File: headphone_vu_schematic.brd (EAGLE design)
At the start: 100 x 80 mm, 20 parts, among them IC1 LM3914V

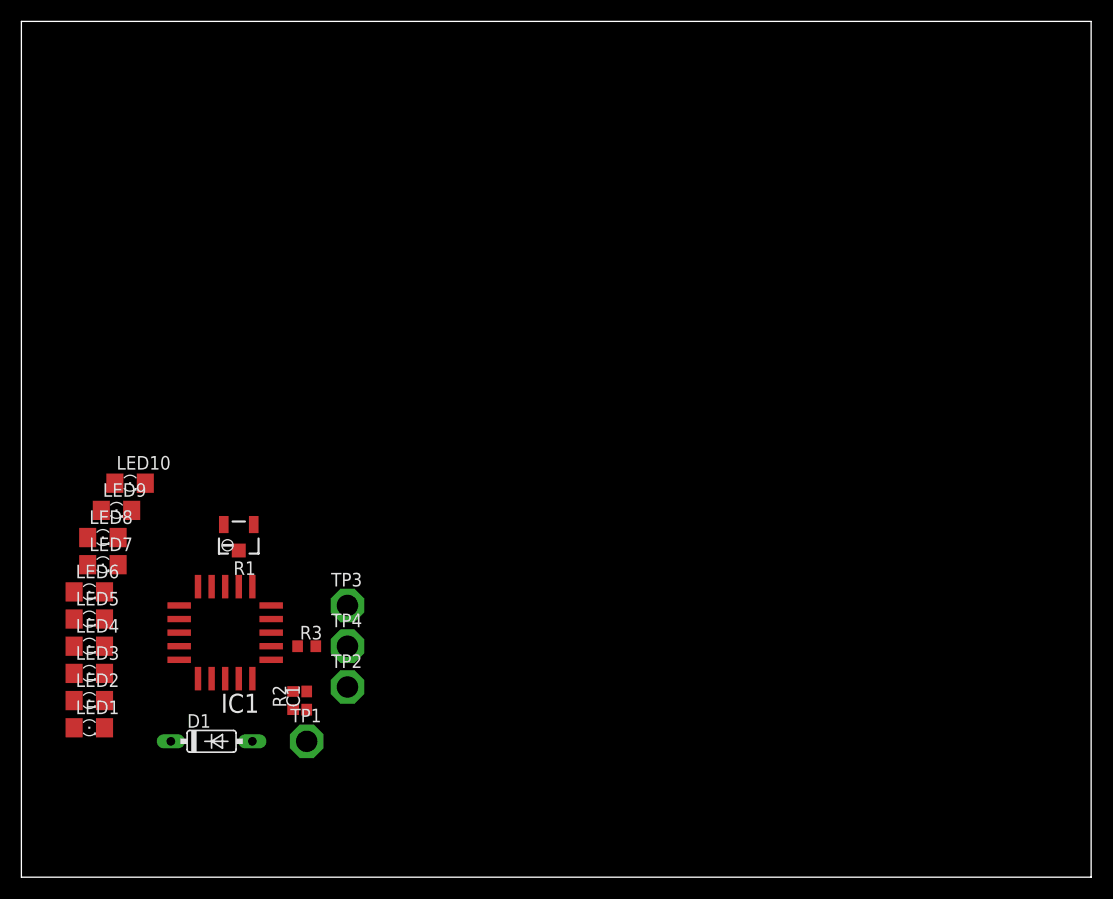
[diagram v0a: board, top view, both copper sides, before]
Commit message: Finished Board
Routed the board.  Everything seems to be in good order.  Single layer,
10 mil min width, 16 mil spacing.  Its hassling me saying there's a
ground not connected, but its all there.
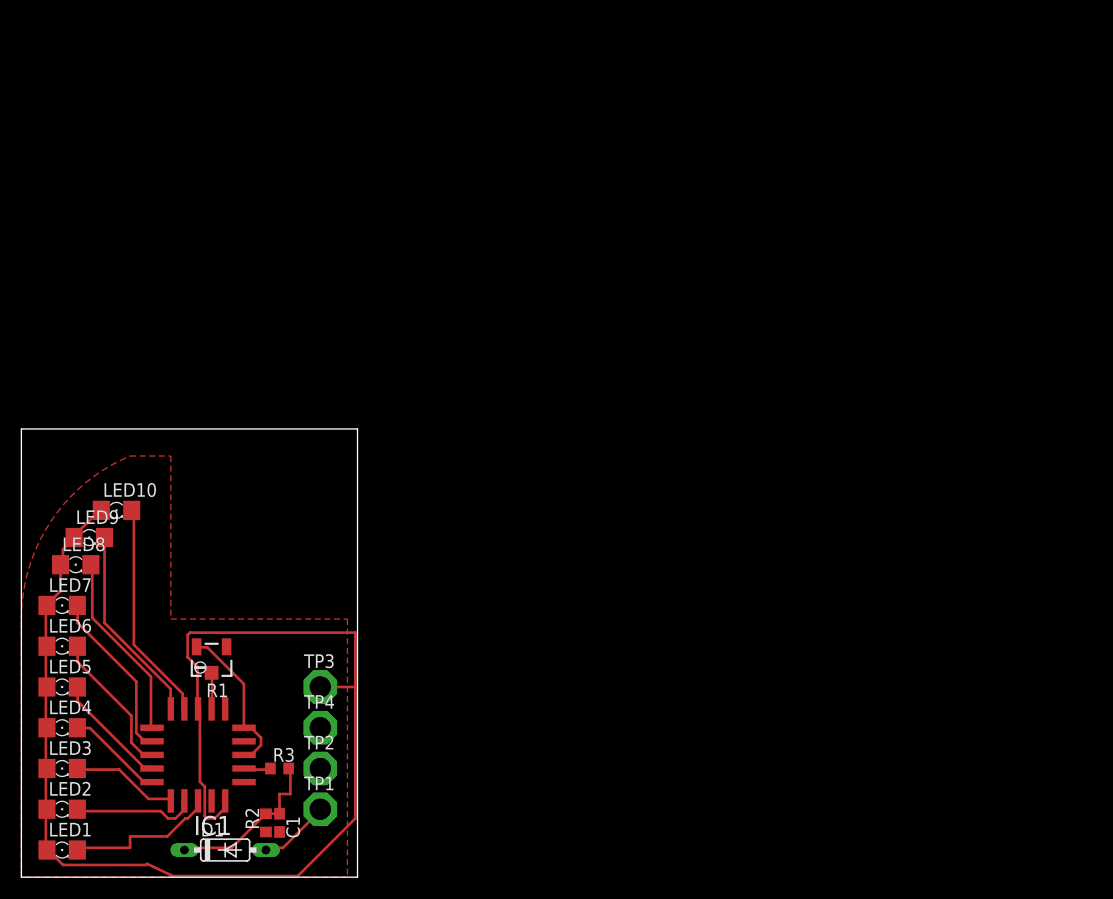
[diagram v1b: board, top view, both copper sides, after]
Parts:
- moved C1 11.7 mm to (24.1, 5.08), turned to 270 degrees
- moved R2 11.7 mm to (22.9, 5.08)
- moved IC1 11.7 mm to (16.5, 11.4)
- moved LED1 11.7 mm to (3.81, 2.54)
- moved R1 11.7 mm to (17.8, 20.3)
- moved R3 11.7 mm to (24.1, 10.2)
- moved LED2 10.5 mm to (3.81, 6.35)
- moved D1 10.2 mm to (19.1, 2.54)
- moved LED3 9.25 mm to (3.81, 10.2)
- moved LED4 8.03 mm to (3.81, 14.0)
- moved TP2 8.03 mm to (27.9, 10.2)
- moved TP4 8.03 mm to (27.9, 14.0)
- moved TP3 8.03 mm to (27.9, 17.8)
- moved LED5 6.84 mm to (3.81, 17.8)
- moved TP1 6.48 mm to (27.9, 6.35)
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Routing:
- net VCC: track 0.00 -> 123.7 mm
- net N$10: track 0.00 -> 20.8 mm
- net N$9: track 0.00 -> 18.6 mm
- net N$8: track 0.00 -> 17.6 mm
- net N$7: track 0.00 -> 16.0 mm
- net N$13: track 0.00 -> 15.7 mm
- net N$11: track 0.00 -> 14.6 mm
- net N$1: track 0.00 -> 14.3 mm
- net N$6: track 0.00 -> 13.5 mm
- net N$2: track 0.00 -> 11.7 mm
- net N$5: track 0.00 -> 10.9 mm
- net N$3: track 0.00 -> 10.1 mm
- net N$4: track 0.00 -> 9.07 mm
- net N$16: track 0.00 -> 6.84 mm
- net N$12: track 0.00 -> 3.41 mm
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- added copper zone on layer 1, net GND
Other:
- board size 100 x 80 mm -> 31.4 x 41.9 mm
